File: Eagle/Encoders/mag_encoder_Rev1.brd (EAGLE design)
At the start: 23.2 x 15 mm, 7 parts, among them IC1 A1203LH

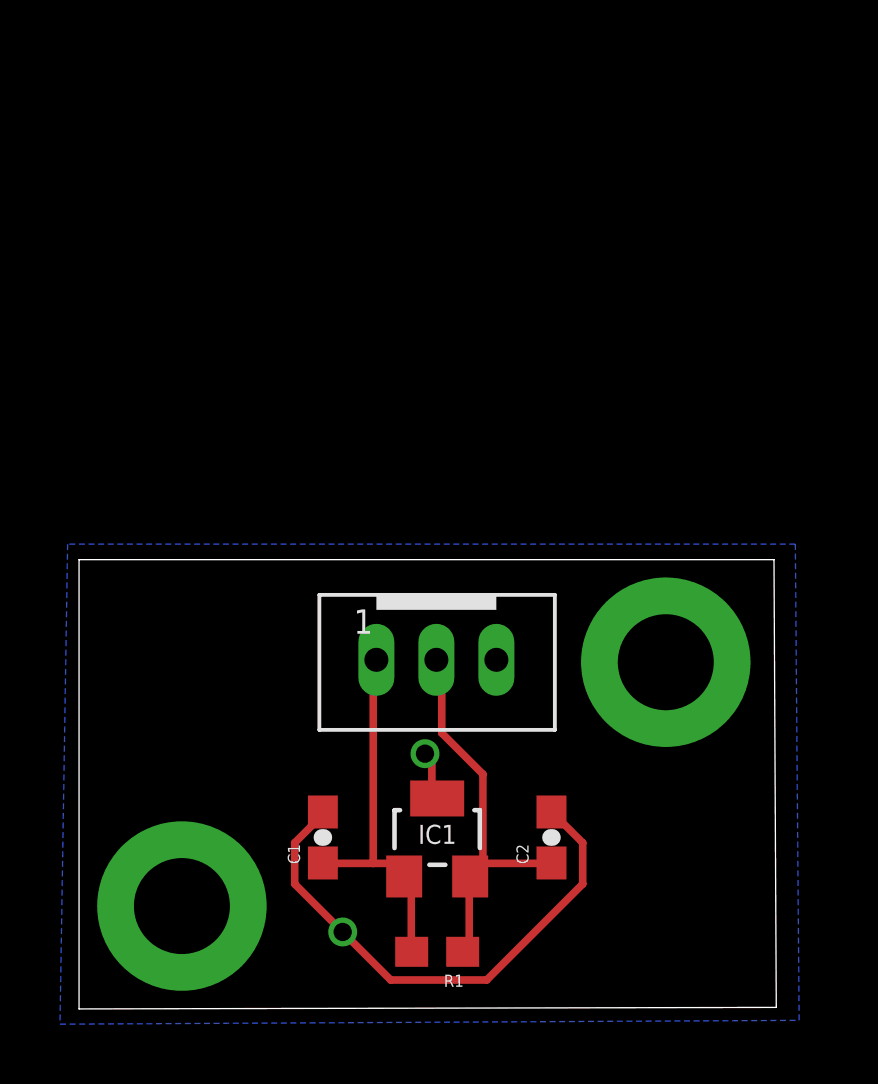
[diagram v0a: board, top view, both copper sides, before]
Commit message: Modified encoder board designs.
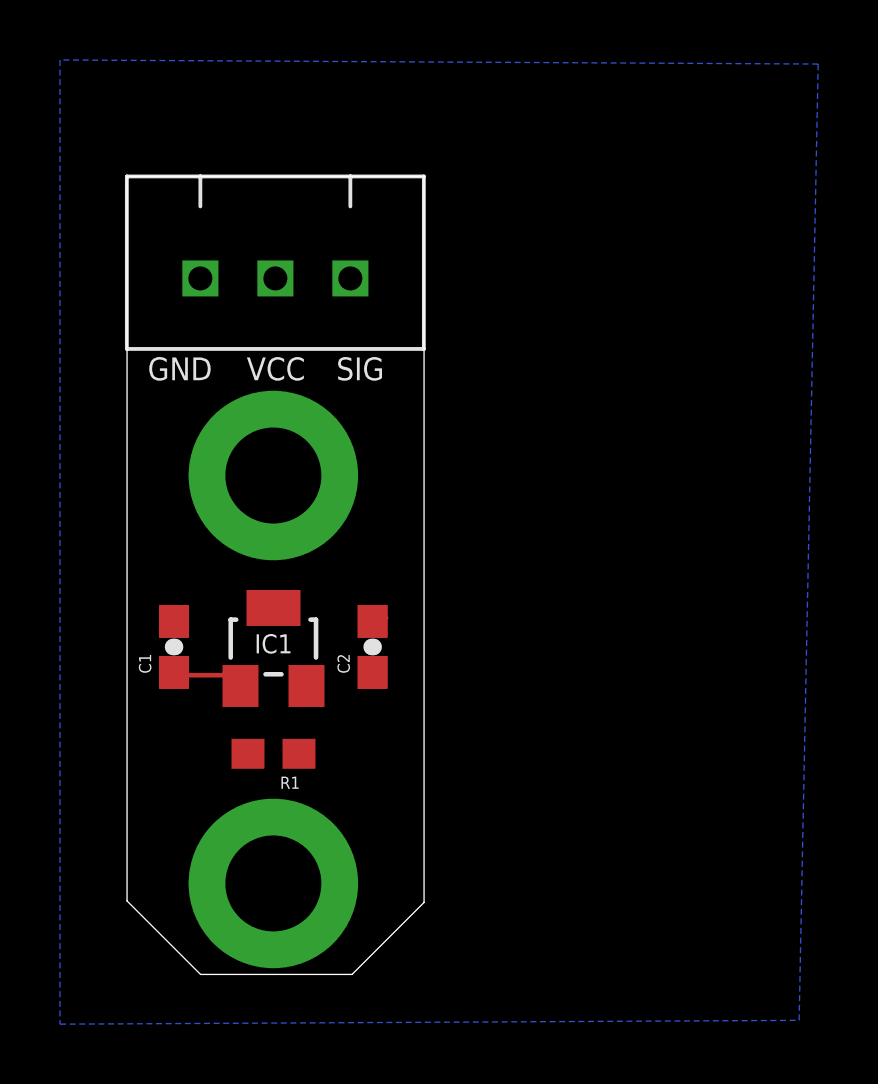
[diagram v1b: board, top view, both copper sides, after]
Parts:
- U$1: value JST-PH_3-PIN_HEADER -> 3_PIN_JST-XH; device Clayton:JST_B3B-PH_HEADER -> Clayton:3_PIN_JST-XH
- moved U$1 16.1 mm to (11.5, 27.7)
- moved U$3 14.5 mm to (6.48, 17.8)
- moved C2 8.71 mm to (9.79, 12.1)
- moved R1 8.57 mm to (6.48, 8.51)
- moved IC1 8.38 mm to (6.48, 12.1)
- moved C1 8.06 mm to (3.17, 12.1)
- moved U$2 3.14 mm to (6.48, 4.18)
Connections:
- removed net VOUT: C2.1, IC1.2, R1.1, U$1.P2
- removed net WIRE: C1.1, IC1.1, R1.2, U$1.P1
- new net SIG: C2.1, IC1.2, R1.1, U$1.P$1
- new net VCC: C1.1, IC1.1, R1.2, U$1.P$2
- net GND: now also U$1.P$3; no longer U$1.P3
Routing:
- net GND: track 20.1 -> 0.86 mm, vias 2 -> 0
- net VOUT: track 13.6 -> 0.00 mm
- net WIRE: track 13.2 -> 0.00 mm
- net VCC: track 0.00 -> 3.22 mm
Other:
- board size 23.2 x 15 mm -> 9.9 x 26.6 mm
- board text added: "GND"
- board text added: "Magnetic Encoder Rev1"
- board text added: "SIG"
- board text added: "VCC"
